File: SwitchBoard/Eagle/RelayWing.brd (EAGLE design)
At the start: 51.7 x 55.9 mm, 30 parts, among them K1 EE2-3TNUH, K2 EE2-3TNUH, K3 EE2-3TNUH, K4 EE2-3TNUH, K5 EE2-3TNUH, U1 ULN2003ANS, U2 ULN2003ANS, U3 MCP23017SS, U4 INA219AID

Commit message: Rev B (start)
First commit for Rev B. See updated Description.
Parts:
- removed I2CHDR: (no value), pinhead:2X02
- removed PWR: (no value), led:1206
- added C3: MUR-1220-CAP, home:CAPC2012
- added JP4, JP5, JP6, JP7: (no value), adafruit:1X01-CLEANBIG
- added POWER: HSMQ-C191, DigiKey:LED3_HSMX-C120
- added R2: 330, home:R01005
- RN1: value CTS746X101 -> CTS746X101102JP
- moved C2 21.9 mm to (14.0, 39.4)
- moved TB5 13.7 mm to (47.0, 5.08)
- moved TB4 13.3 mm to (29.2, 5.08)
- moved TB3 13.0 mm to (11.4, 5.08)
- moved R1 12.1 mm to (15.7, 49.4)
- moved RN1 12.0 mm to (49.1, 26.3), turned to 270 degrees
- moved A0 11.5 mm to (3.81, 44.5)
- moved A1 11.5 mm to (7.62, 44.5)
- moved C1 11.5 mm to (26.7, 29.2), turned to 270 degrees
- moved JP2 11.5 mm to (26.7, 22.9)
- moved JP3 11.5 mm to (31.8, 38.1)
- moved K1 11.5 mm to (44.5, 47.0)
- moved K2 11.5 mm to (27.9, 47.0)
- moved MS1 11.5 mm to (1.27, 19.1)
- moved U1 11.5 mm to (8.89, 31.8)
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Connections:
- net N$16 renamed K1A-NO
- net N$17 renamed K2A-NO
- net N$2 renamed K4B-NO
- net N$24 renamed K1-SET
- net N$25 renamed K4B-NC
- net N$26 renamed K2A-CO
- net N$27 renamed K2A-NC
- net N$28 renamed K1A-NC
- net N$29 renamed K1B-NC
- net N$30 renamed K1A-CO
- net N$32 renamed K1B-CO
- net N$33 renamed K2B-CO
- net N$34 renamed K1-RESET
- net N$35 renamed K1B-NO
- net N$36 renamed K2-SET
- net N$37 renamed K2-RESET
- net N$38 renamed K3-SET
- net N$39 renamed K3-RESET
- net N$40 renamed K4A-CO
- net N$42 renamed K4A-N0
- net N$43 renamed K5A-CO
- net N$44 renamed K5A-NO
- net N$45 renamed K5B-NC
- net N$46 renamed K5B-CO
- net N$47 renamed K5B-NO
- net N$49 renamed K4B-CO
- net N$50 renamed K5A-NC
- net N$52 renamed K3A-NO
- net N$53 renamed K3A-NC
- net N$54 renamed K3A-CO
- net N$55 renamed K3B-NO
- net N$56 renamed K3B-NC
- net N$57 renamed K3B-CO
- net N$58 renamed K4-SET
- net N$59 renamed K4-RESET
- net N$60 renamed K5-SET
- net N$72 renamed K2B-NO
- net N$73 renamed K5-RESET
- net N$78 renamed K2B-NC
- net N$79 renamed K4A-NC
- removed net N$18: JP2.1, MS1.1, RESET.P$2, U3.18
- new net N$31: R2.2, RESET.P$1
- new net RESET/: C3.2, JP2.1, MS1.1, RESET.P$2, RN1.9, U3.18
- net 3V: now also JP4.1, POWER.2; no longer I2CHDR.3, PWR.A
- net GND: now also C3.1, JP5.1, POWER.1, R2.1; no longer I2CHDR.1, PWR.C, RESET.P$1
- net SCL: now also JP6.1; no longer I2CHDR.2
- net SDA: now also JP7.1; no longer I2CHDR.4
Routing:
- net RESET/: track 0.00 -> 90.0 mm, vias 0 -> 3
- net N$18: track 38.5 -> 0.00 mm, vias 2 -> 0
- net N$66: track 16.8 -> 51.9 mm, vias 2 -> 5
- net 3V: track 256.6 -> 224.6 mm, vias 8 -> 9
- net GND: track 158.2 -> 127.2 mm, vias 9 -> 4
- net N$70: track 57.7 -> 81.8 mm, vias 6 -> 4
- net N$68: track 54.3 -> 32.3 mm, vias 4 -> 2
- net N$69: track 24.1 -> 44.4 mm, vias 2 -> 4
- net N$71: track 36.9 -> 17.7 mm, vias 0 -> 2
- net A1: track 58.6 -> 76.5 mm, vias 5 -> 3
- net N$80: track 19.8 -> 36.5 mm, vias 3 -> 4
- net A0: track 80.2 -> 66.0 mm, vias 7 -> 5
- net N$77: track 23.6 -> 37.7 mm
- net N$63: track 22.7 -> 36.6 mm
- net SDA: track 64.6 -> 78.0 mm
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- added copper zone on layer 16, net GND
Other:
- board size 51.7 x 55.9 mm -> 55.5 x 58.4 mm
- board text added: "3V3"
- board text added: "Current Sensor: 2A @ 0-24V DC Only"
- board text added: "Relays: 2A @ +/-24V AC/DC"
- board text removed: "3V"
- board text removed: "Current Sensor: 2A @ 0-24V DC ONLY"
- board text removed: "I2C ADDR"
- board text removed: "Relay 1"
- board text removed: "Relay 2"
- board text removed: "Relay 3"
- board text removed: "Relay 4"
- board text removed: "Relay 5"
- board text removed: "Relay Switches: 2A @ +/- 24V AC/DC"

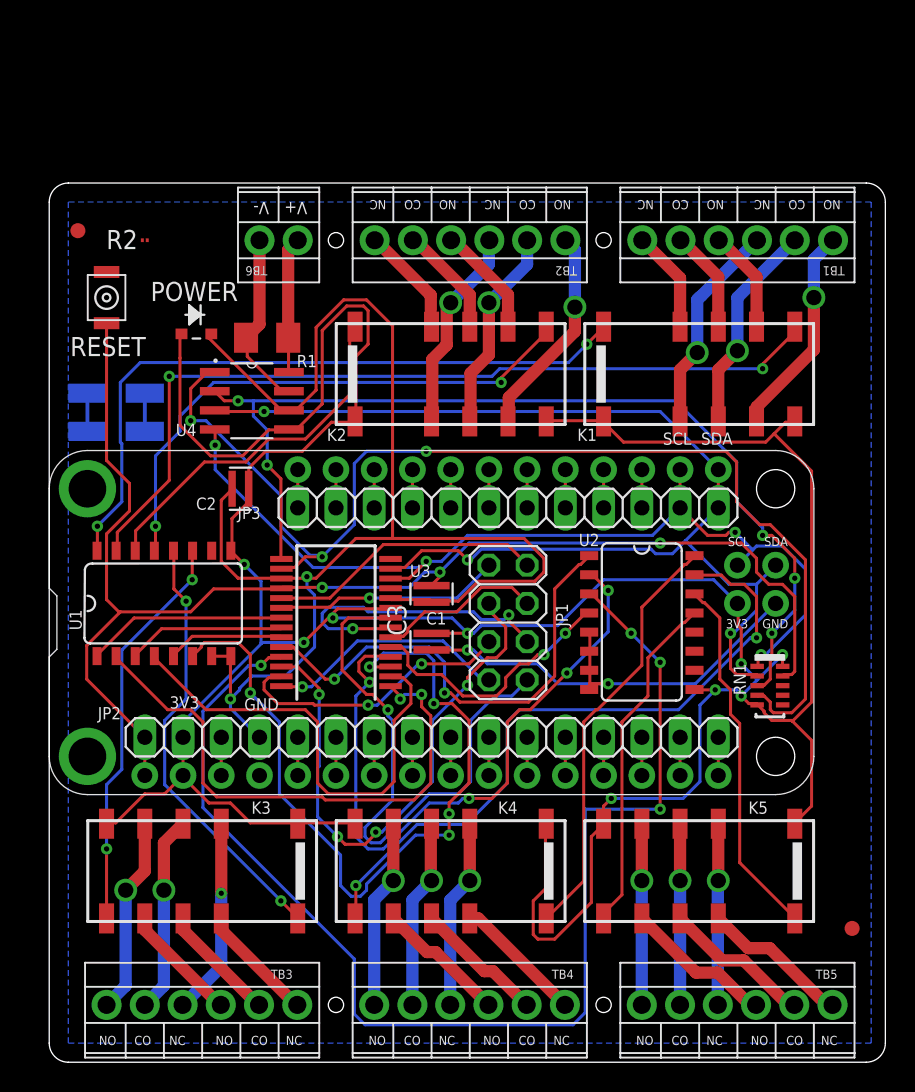
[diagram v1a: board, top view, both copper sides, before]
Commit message: more routing
More routing and clean DRC items. Some airwires remain.
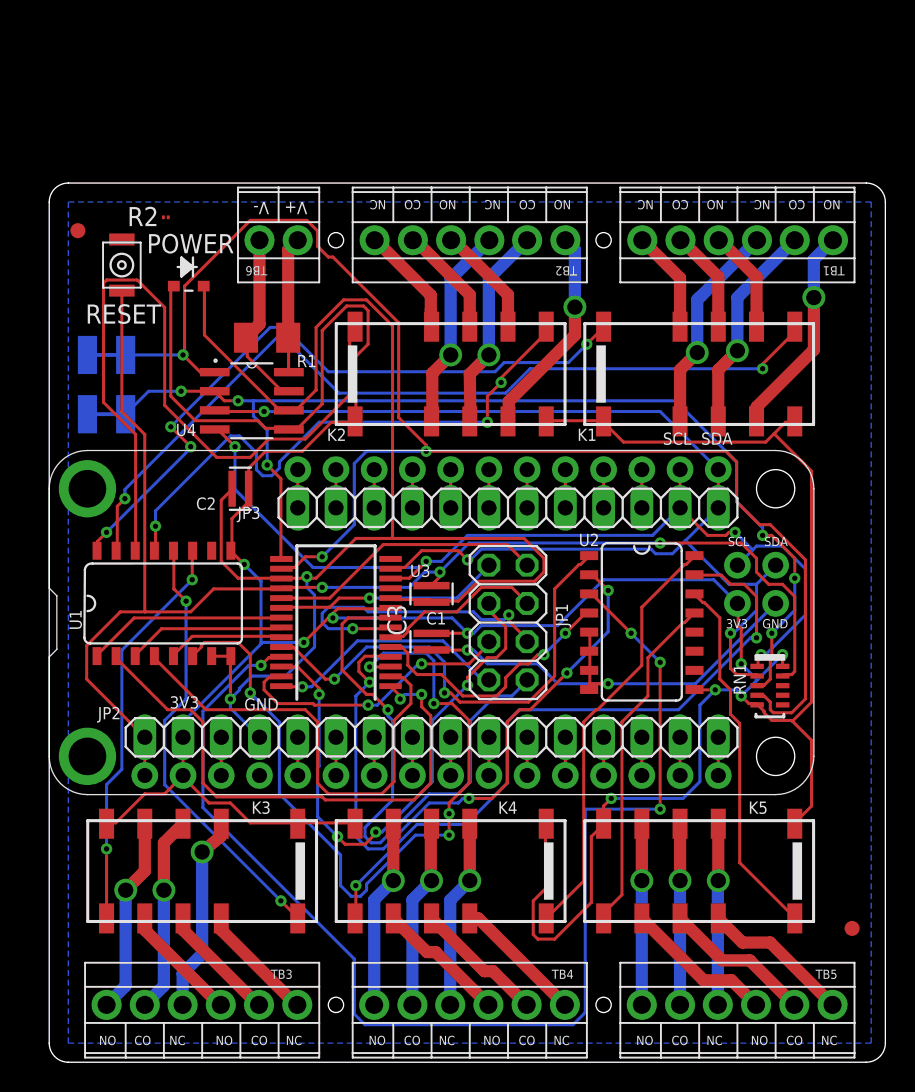
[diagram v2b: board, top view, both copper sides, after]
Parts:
- moved A1 4.58 mm to (5.08, 48.3), turned to 0 degrees
- moved POWER 3.22 mm to (10.5, 52.8)
- moved RESET 2.39 mm to (6.10, 54.2)
- moved R2 2.07 mm to (9.02, 57.4)
- moved A0 1.28 mm to (5.08, 44.3), turned to 0 degrees
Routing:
- net K2-SET: track 24.0 -> 50.2 mm
- net A1: track 76.5 -> 98.4 mm
- net A0: track 66.0 -> 72.5 mm, vias 5 -> 6
- net GND: track 127.2 -> 132.6 mm
- net K2-RESET: track 36.9 -> 38.3 mm, vias 2 -> 3
- net 3V: track 224.6 -> 225.8 mm
- net K2B-NC: track 6.21 -> 7.35 mm
- net RESET/: track 90.0 -> 91.1 mm
- net K1-RESET: track 56.4 -> 56.9 mm
- net K1-SET: track 45.6 -> 45.4 mm, vias 2 -> 4

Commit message: resistor & routing changes
Added LED resistor, resized resisitor to 0603, relocate reset cap.
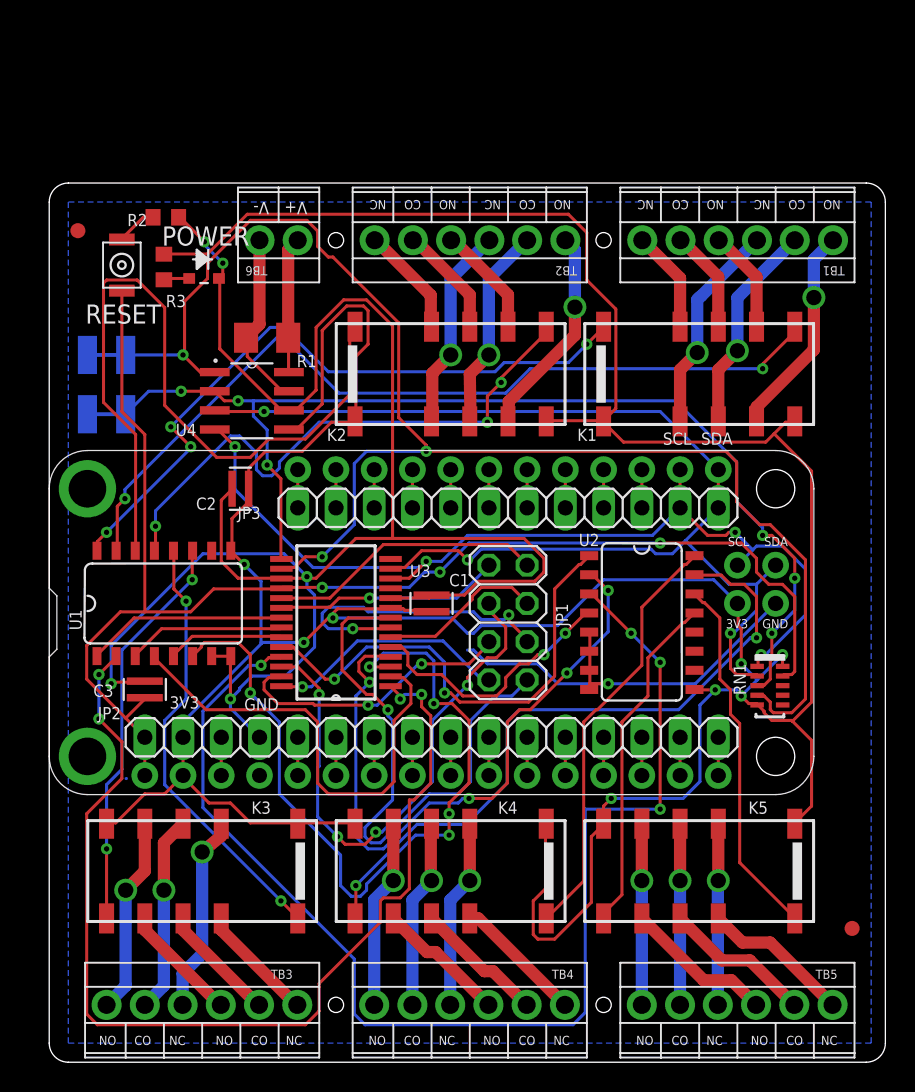
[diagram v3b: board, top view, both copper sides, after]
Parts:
- added R3: 75, home:R0603
- R2: device home:R01005 -> home:R0603
- moved C3 20.1 mm to (7.62, 26.0), turned to 270 degrees
- moved C1 2.54 mm to (26.7, 31.8), turned to 90 degrees
- moved POWER 1.14 mm to (11.6, 53.3)
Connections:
- net N$62 renamed GPA0
- net N$63 renamed GPB0
- net N$64 renamed GPA1
- net N$65 renamed GPA2
- net N$66 renamed GPB2
- net N$67 renamed GPB1
- net N$68 renamed GPA3
- net N$69 renamed GPB3
- net N$70 renamed GPA4
- net N$71 renamed GPB4
- net N$74 renamed GPA7
- net N$75 renamed GPB5
- net N$76 renamed GPB6
- net N$77 renamed GPB7
- net N$80 renamed GPA5
- net N$81 renamed GPA6
- new net N$2: POWER.2, R3.1
- net 3V: now also R3.2; no longer POWER.2
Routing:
- net GPB0: track 36.6 -> 70.3 mm, vias 2 -> 4
- net 3V: track 225.8 -> 253.4 mm, vias 9 -> 8
- net GND: track 132.6 -> 156.6 mm, vias 4 -> 6
- net N$31: track 0.00 -> 2.71 mm
- net N$2: track 0.00 -> 1.73 mm
- net RESET/: track 91.1 -> 91.9 mm

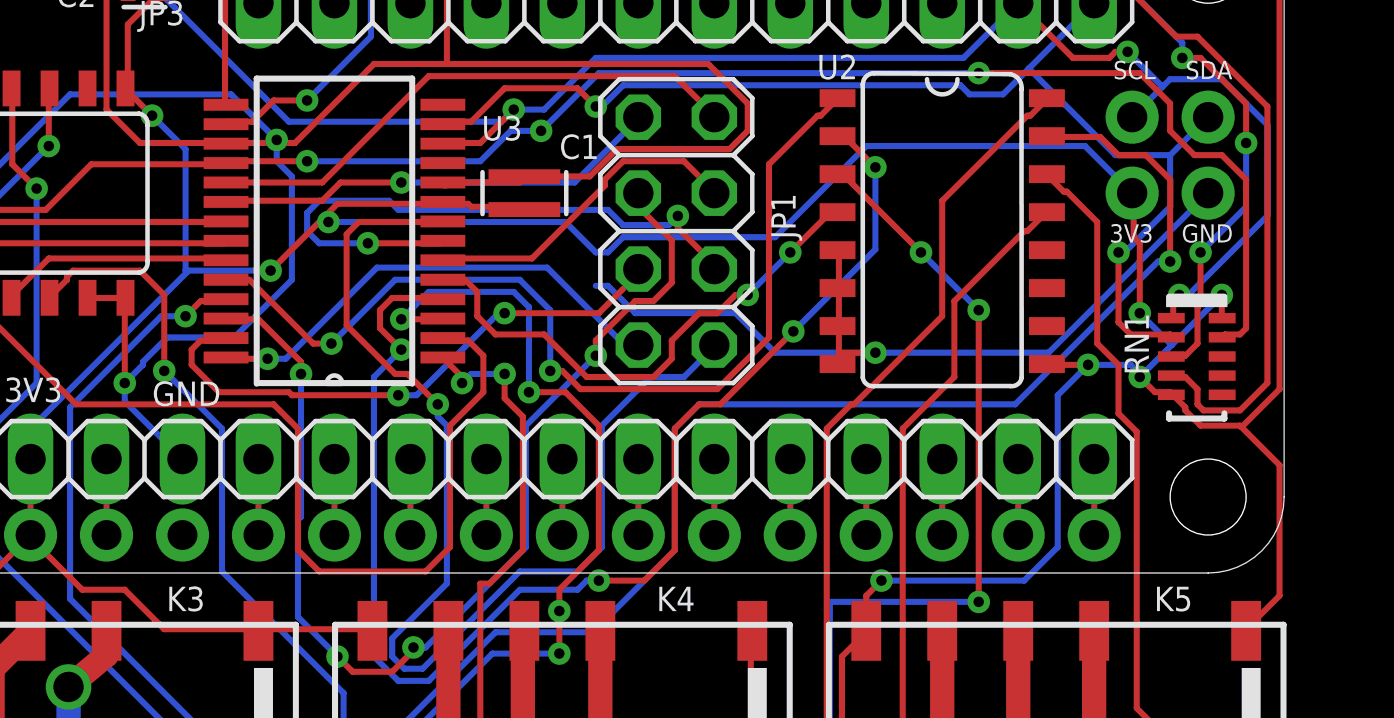
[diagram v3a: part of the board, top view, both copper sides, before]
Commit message: board 100% routed
DRC clean with some very minor exceptions.
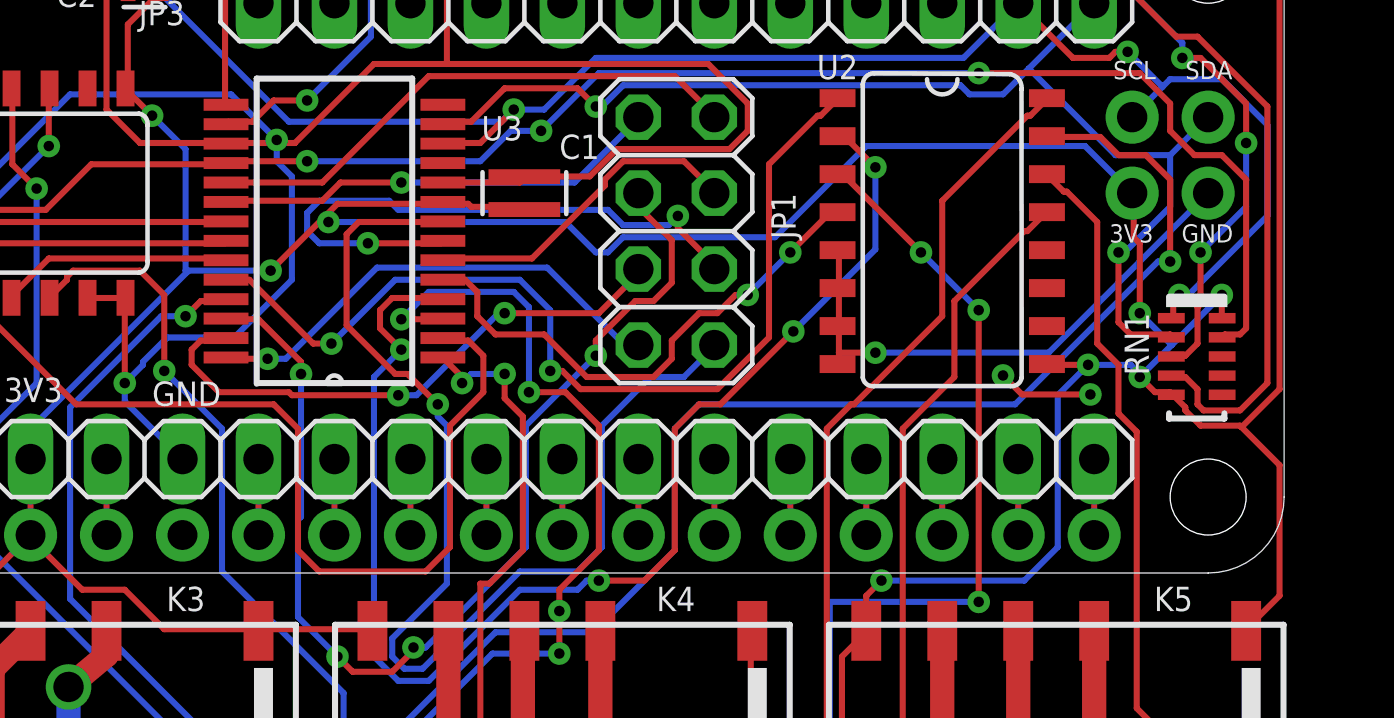
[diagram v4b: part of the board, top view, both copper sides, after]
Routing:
- net GND: track 156.6 -> 148.2 mm, vias 6 -> 8
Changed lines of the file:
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@@
 <setting verticaltext="up"/>
 </settings>
-<grid distance="100" unitdist="mil" unit="mil" style="lines" multiple="1" display="yes" altdistance="10" altunitdist="mil" altunit="mil"/>
+<grid distance="100" unitdist="mil" unit="mil" style="lines" multiple="1" display="yes" altdistance="5" altunitdist="mil" altunit="mil"/>
 <layers>
 <layer number="1" name="Top" color="4" fill="1" visible="yes" active="yes"/>
@@
 <wire x1="15.24" y1="22.86" x2="13.3096" y2="24.7904" width="0.2032" layer="16"/>
 <wire x1="13.3096" y1="28.1432" x2="13.335" y2="28.25" width="0.2032" layer="1"/>
-<wire x1="29.464" y1="28.6512" x2="29.0576" y2="28.6512" width="0.2032" layer="16"/>
-<wire x1="30.3784" y1="27.7368" x2="29.464" y2="28.6512" width="0.2032" layer="16"/>
-<wire x1="33.7312" y1="27.7368" x2="30.3784" y2="27.7368" width="0.2032" layer="16"/>
-<wire x1="35.052" y1="26.416" x2="33.7312" y2="27.7368" width="0.2032" layer="16"/>
 <wire x1="44.196" y1="26.416" x2="38.4048" y2="26.416" width="0.2032" layer="16"/>
-<wire x1="38.4048" y1="26.416" x2="35.052" y2="26.416" width="0.2032" layer="16"/>
 <wire x1="49.53" y1="31.75" x2="44.196" y2="26.416" width="0.2032" layer="16"/>
 <wire x1="38.4048" y1="26.416" x2="37.1856" y2="26.416" width="0.2032" layer="1"/>
@@
 <wire x1="16.6624" y1="44.6024" x2="17.1704" y2="44.6024" width="0.2032" layer="1"/>
 <wire x1="17.1704" y1="44.6024" x2="17.1958" y2="44.577" width="0.2032" layer="1"/>
-<wire x1="23.9776" y1="32.004" x2="23.945" y2="32.105" width="0.2032" layer="1"/>
 <wire x1="13.8176" y1="33.4264" x2="16.6624" y2="33.4264" width="0.2032" layer="1"/>
 <wire x1="12.7" y1="34.544" x2="13.8176" y2="33.4264" width="0.2032" layer="1"/>
@@
 <wire x1="16.6624" y1="44.6024" x2="17.1958" y2="44.577" width="0.2032" layer="1"/>
 <wire x1="16.5608" y1="44.6024" x2="17.1958" y2="44.577" width="0.2032" layer="1"/>
-<wire x1="49.4792" y1="31.9024" x2="49.53" y2="31.75" width="0.2032" layer="16"/>
-<wire x1="49.5808" y1="31.8008" x2="49.53" y2="31.75" width="0.2032" layer="16"/>
-<wire x1="49.5808" y1="31.8008" x2="49.63159375" y2="31.8516125" width="0.2032" layer="16"/>
-<wire x1="15.24" y1="20.5232" x2="15.24" y2="20.32" width="0.2032" layer="16"/>
-<wire x1="15.24" y1="20.4216" x2="15.34159375" y2="20.4216125" width="0.2032" layer="16"/>
-<wire x1="15.3416" y1="20.4216" x2="15.24" y2="20.32" width="0.2032" layer="16"/>
 <wire x1="15.3416" y1="20.4216" x2="15.34159375" y2="20.4216125" width="0.2032" layer="16"/>
 <wire x1="12.5984" y1="48.6664" x2="12.5984" y2="53.34" width="0.2032" layer="1"/>
@@
 <via x="5.3848" y="26.416" extent="1-16" drill="0.35"/>
 <wire x1="6.4008" y1="20.1168" x2="6.3754" y2="20.1168" width="0.2032" layer="16"/>
-<wire x1="24.046" y1="32.004" x2="23.945" y2="32.105" width="0.2032" layer="1"/>
-<wire x1="24.0792" y1="32.1056" x2="23.945" y2="32.105" width="0.2032" layer="1"/>
 <wire x1="26.5176" y1="32.1056" x2="24.0792" y2="32.1056" width="0.2032" layer="1"/>
 <wire x1="26.6192" y1="32.2072" x2="26.5176" y2="32.1056" width="0.2032" layer="1"/>
-<wire x1="24.0792" y1="32.1056" x2="23.945" y2="32.105" width="0.2032" layer="1"/>
 <wire x1="26.6192" y1="32.2072" x2="26.67" y2="32.3" width="0.2032" layer="1"/>
 <wire x1="28.8544" y1="32.3088" x2="26.7208" y2="32.3088" width="0.2032" layer="1"/>
@@
 <wire x1="24.0792" y1="36.068" x2="32.8168" y2="36.068" width="0.2032" layer="1"/>
 <wire x1="26.7208" y1="32.3088" x2="26.67" y2="32.3" width="0.2032" layer="1"/>
-<wire x1="15.24" y1="20.5232" x2="15.24" y2="20.32" width="0.2032" layer="16"/>
-<wire x1="28.8544" y1="32.3088" x2="29.0576" y2="28.6512" width="0" layer="19" extent="1-16"/>
+<via x="42.672" y="25.654" extent="1-16" drill="0.35"/>
+<via x="45.593" y="25.019" extent="1-16" drill="0.35"/>
+<wire x1="45.593" y1="25.019" x2="43.307" y2="25.019" width="0.2032" layer="1"/>
+<wire x1="43.307" y1="25.019" x2="42.672" y2="25.654" width="0.2032" layer="1"/>
+<wire x1="24.0792" y1="32.1056" x2="23.9776" y2="32.1056" width="0.2032" layer="1"/>
+<wire x1="23.9776" y1="32.1056" x2="23.945" y2="32.105" width="0.2032" layer="1"/>
 </signal>
 <signal name="3V">
@@
 <contactref element="U3" pad="6"/>
 <contactref element="JP1" pad="4"/>
-<wire x1="26.924" y1="29.5656" x2="24.0792" y2="29.5656" width="0.2032" layer="1"/>
+<wire x1="26.924" y1="29.5656" x2="23.9776" y2="29.5656" width="0.2032" layer="1"/>
 <wire x1="29.3624" y1="32.004" x2="26.924" y2="29.5656" width="0.2032" layer="1"/>
 <wire x1="29.3624" y1="32.2072" x2="29.3624" y2="32.004" width="0.2032" layer="1"/>
@@
 <wire x1="33.02" y1="31.8008" x2="32.004" y2="32.8168" width="0.2032" layer="1"/>
 <wire x1="33.02" y1="31.8008" x2="33.02" y2="31.75" width="0.2032" layer="1"/>
-<wire x1="24.0792" y1="29.5656" x2="23.9776" y2="29.5656" width="0.2032" layer="1"/>
 <wire x1="23.9776" y1="29.5656" x2="23.945" y2="29.505" width="0.2032" layer="1"/>
 </signal>
